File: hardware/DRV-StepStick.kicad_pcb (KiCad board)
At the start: 2 copper layers, 36.7 x 39.4 mm, 22 parts, among them J1 PCIe_Stepper, J2 Motor, J3 StepStickL, J4 StepStickR, J5 Conn_01x04, J6 SPI Mode, J7 Conn_01x02, U2 74LVC1G06

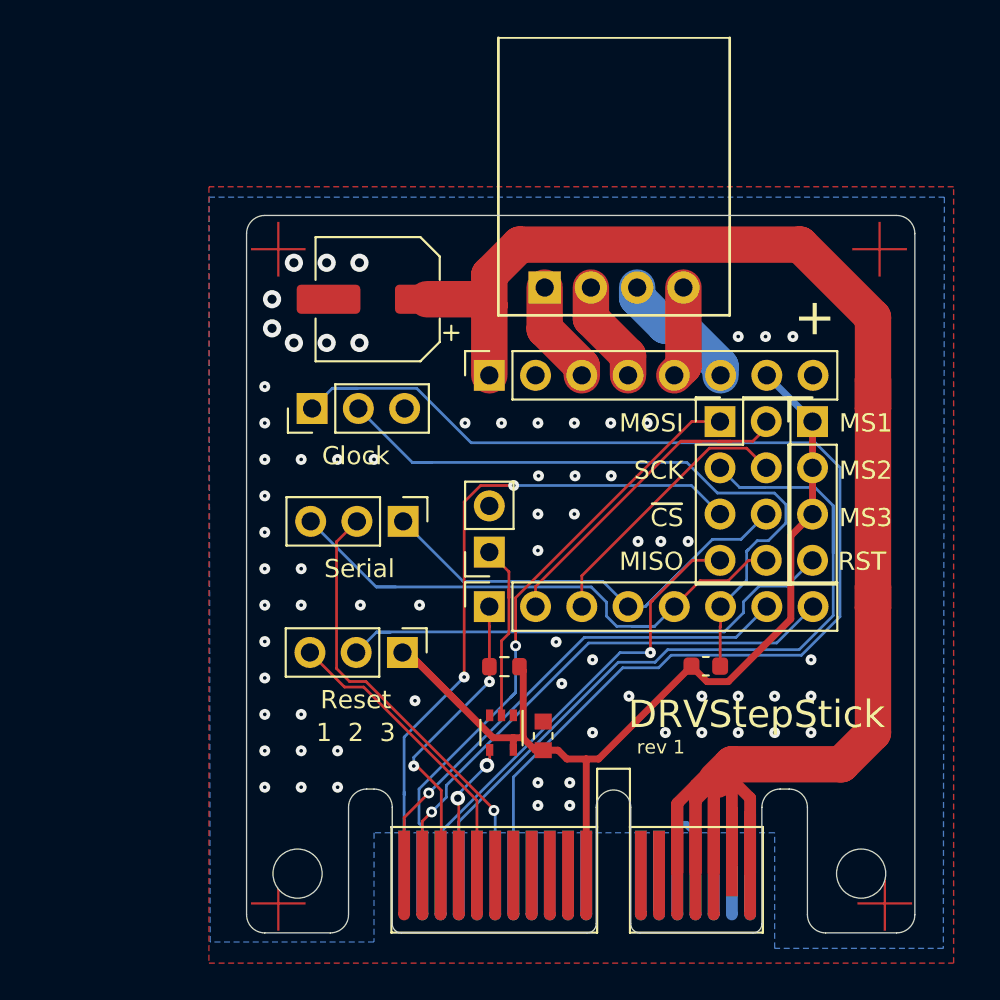
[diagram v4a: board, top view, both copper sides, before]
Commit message: Move the configuration jumpers out of the way.
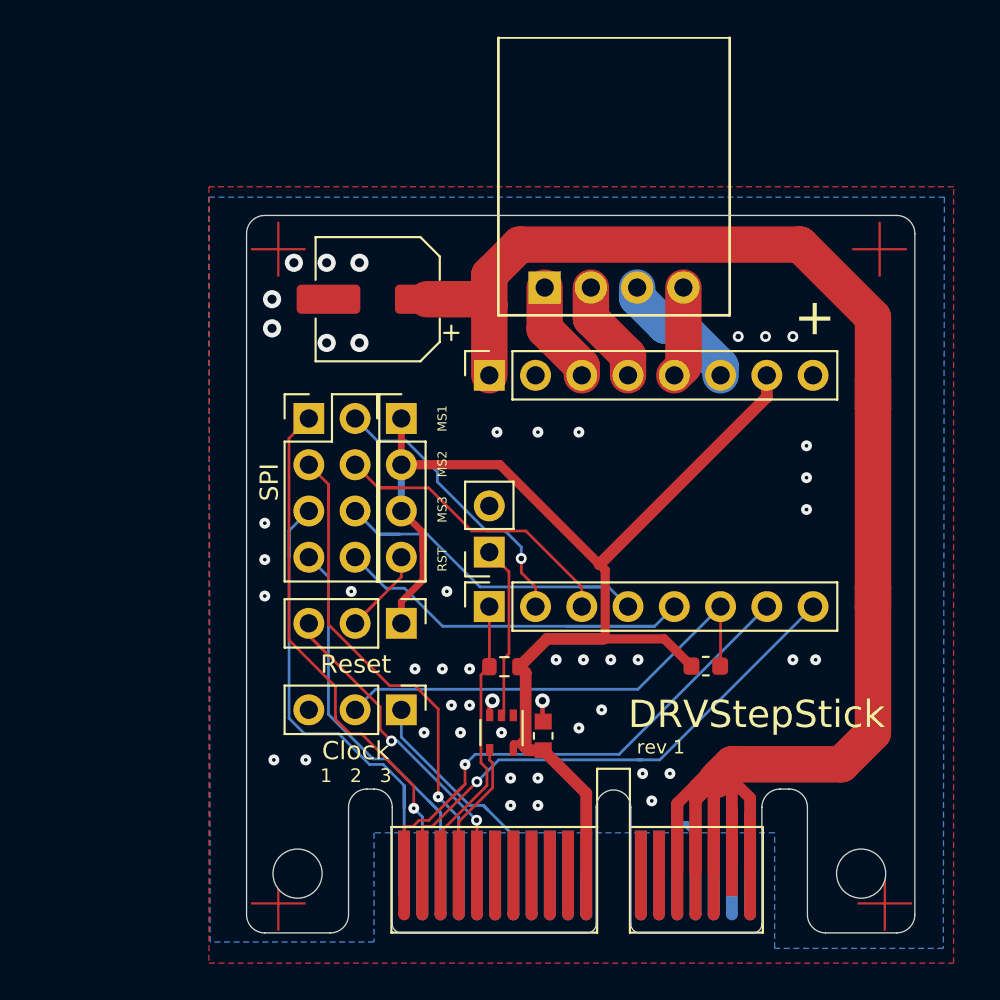
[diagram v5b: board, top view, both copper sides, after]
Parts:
- removed JP2: Serial, Connector_PinHeader_2.54mm:PinHeader_1x03_P2.54mm_Vertical
- moved J5 22.6 mm to (117.5, 85.8)
- moved J6 22.6 mm to (112.4, 85.8)
- moved JP3 17.3 mm to (117.5, 101.8), turned to -90 degrees
- moved JP4 1.60 mm to (117.5, 97.0)
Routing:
- net /CLOCK: track 67.7 -> 12.3 mm
- net /SERIAL: track 23.9 -> 0.00 mm, vias 1 -> 0
- net Net-(J5-Pad4): track 28.3 -> 6.47 mm
- net /SCK: track 45.1 -> 28.0 mm, vias 0 -> 1
- net VCC: track 57.5 -> 70.6 mm
- net /SLP/DCO/CLK/UART: track 37.6 -> 25.7 mm
- net /~CS: track 36.4 -> 26.6 mm, vias 2 -> 0
- net /MS3/~CS/UART: track 28.9 -> 20.0 mm
- net /RST/MISO/UART: track 31.7 -> 24.4 mm
- net /MOSI: track 33.0 -> 28.9 mm
- net /MISO: track 25.5 -> 21.7 mm, vias 1 -> 0
- net /MS1/MOSI: track 19.5 -> 16.0 mm, vias 0 -> 1
- net /~ST_RESET: track 16.5 -> 19.4 mm, vias 0 -> 2
- net /MS2/SCK: track 15.2 -> 17.6 mm
- net GND: track 15.2 -> 17.3 mm, vias 70 -> 48
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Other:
- board text added: "SPI"
- board text removed: "MISO"
- board text removed: "MOSI"
- board text removed: "SCK"
- board text removed: "Serial"
- board text removed: "~CS"
